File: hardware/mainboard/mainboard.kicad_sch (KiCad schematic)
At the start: 82 parts, among them J1 USB_C_Receptacle_USB2.0_16P, J2 Conn_01x03_Pin, J3 Barrel_Jack_MountingPin, J4 Conn_01x04_Socket, J5 Conn_01x04_Socket, J6 Screw_Terminal_01x02, J7 Conn_01x02_Socket, J8 Conn_01x02_Socket, J9 Conn_01x04_Socket, Q1 BTN8982TA, Q2 AO3400A, Q3 AO3400A, Q6 BTN8982TA, U1 ESP32-S3-WROOM-1, U2 USBLC6-2SC6, U3 AP2112K-3.3, U4 TPS2116DRL, U5 TPS62161DSG

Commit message: finished component placement
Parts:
- J9: footprint Connector_PinHeader_2.54mm:PinHeader_1x04_P2.54mm_Vertical -> Connector_PinSocket_2.54mm:PinSocket_1x04_P2.54mm_Vertical
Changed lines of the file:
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@@
 			)
 		)
-		(property "Footprint" "Connector_PinHeader_2.54mm:PinHeader_1x04_P2.54mm_Vertical"
+		(property "Footprint" "Connector_PinSocket_2.54mm:PinSocket_1x04_P2.54mm_Vertical"
 			(at 184.15 95.25 0)
 			(effects

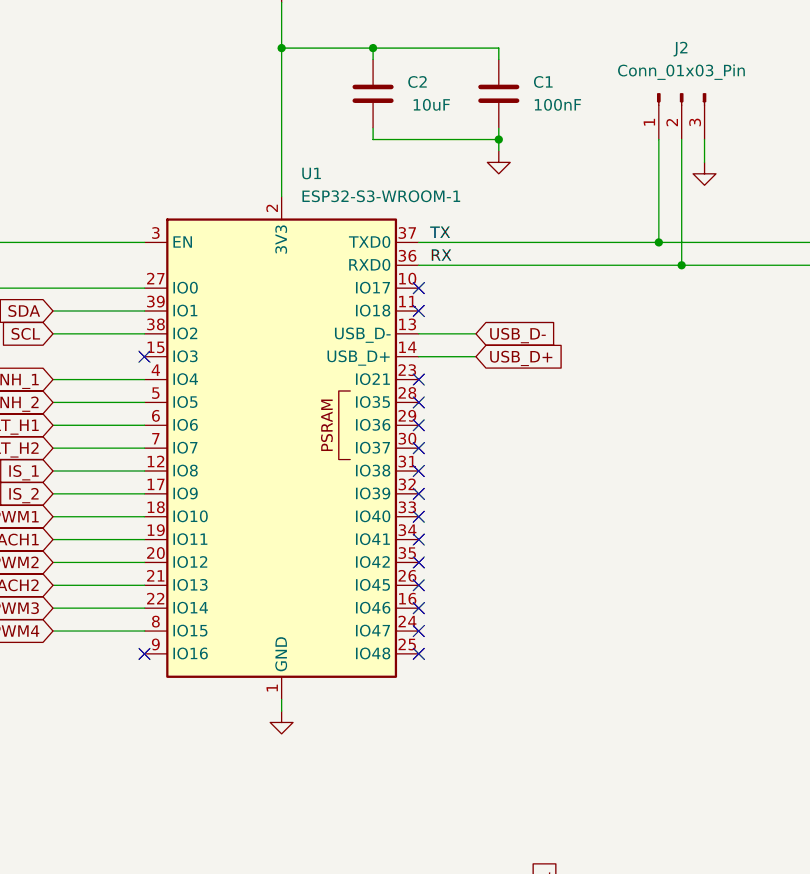
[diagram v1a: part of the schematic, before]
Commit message: signal routing for pwm fans and h-bridge
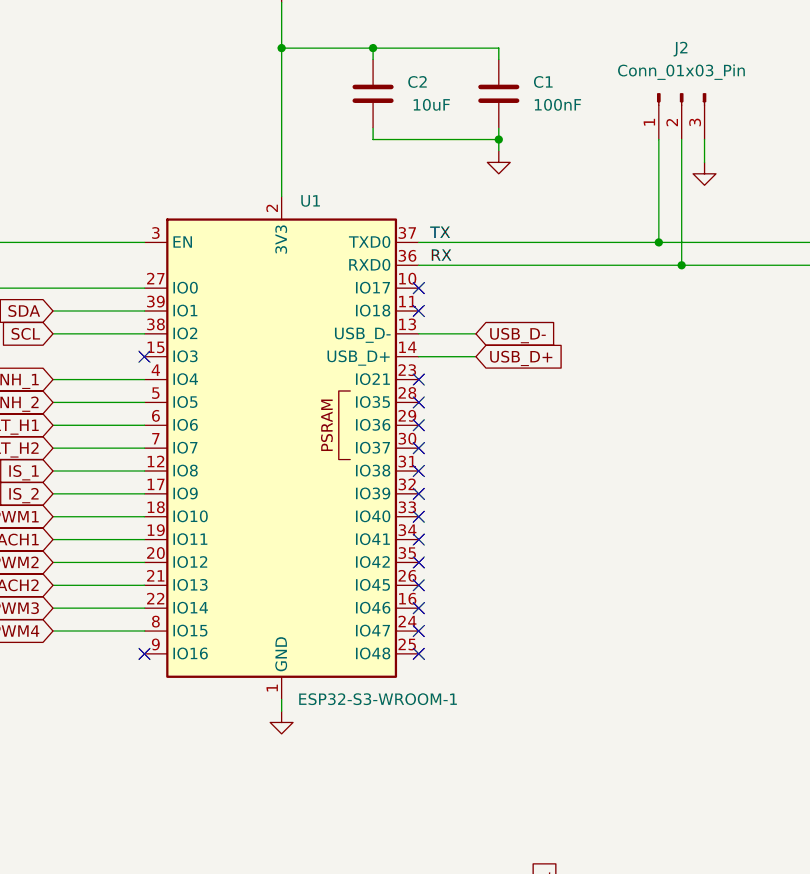
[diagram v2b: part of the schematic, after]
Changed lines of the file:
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@@
 		(on_board yes)
 		(dnp no)
-		(fields_autoplaced yes)
 		(property "Reference" "U1"
-			(at 91.0433 45.72 0)
+			(at 90.932 48.768 0)
 			(effects
 				(font
@@
 		)
 		(property "Value" "ESP32-S3-WROOM-1"
-			(at 91.0433 48.26 0)
+			(at 90.678 104.14 0)
 			(effects
 				(font

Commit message: revised routing and power stage routing
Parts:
- added H1, H2, H3: MountingHole_Pad, MountingHole:MountingHole_2.2mm_M2_Pad_TopBottom, symbol Mechanical:MountingHole_Pad
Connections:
- net GND: now also H1.1, H2.1, H3.1

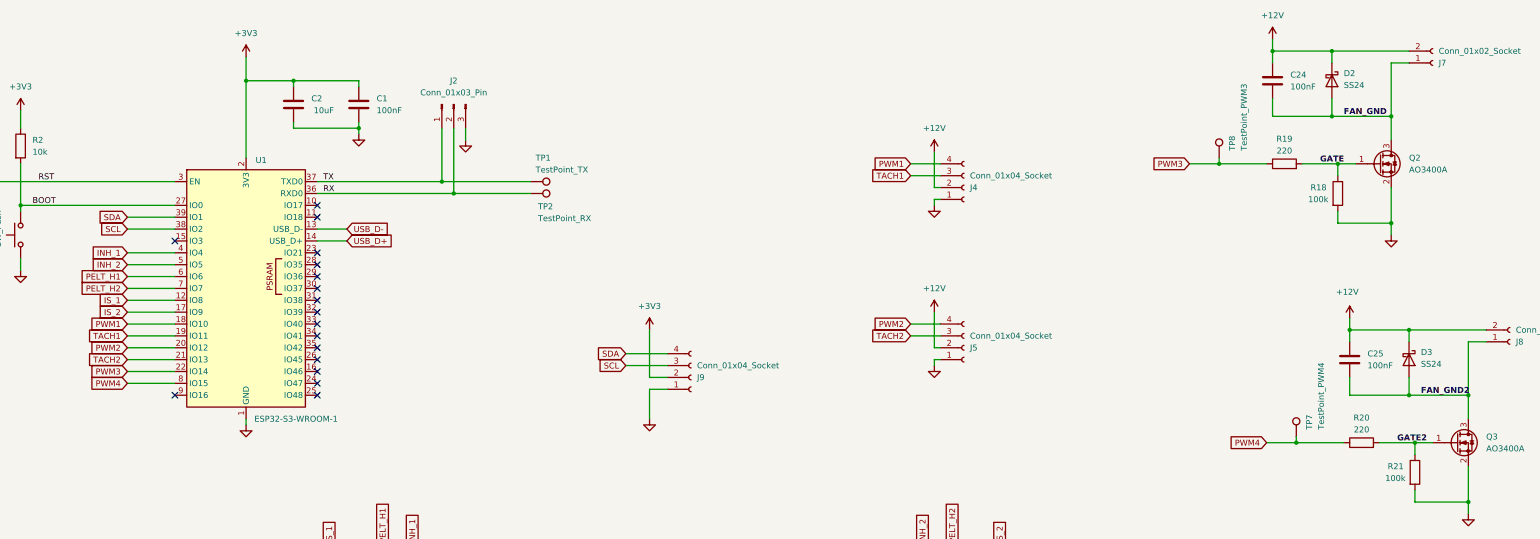
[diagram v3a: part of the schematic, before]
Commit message: routing reworks; adjusted display position, silkscreen adjustments
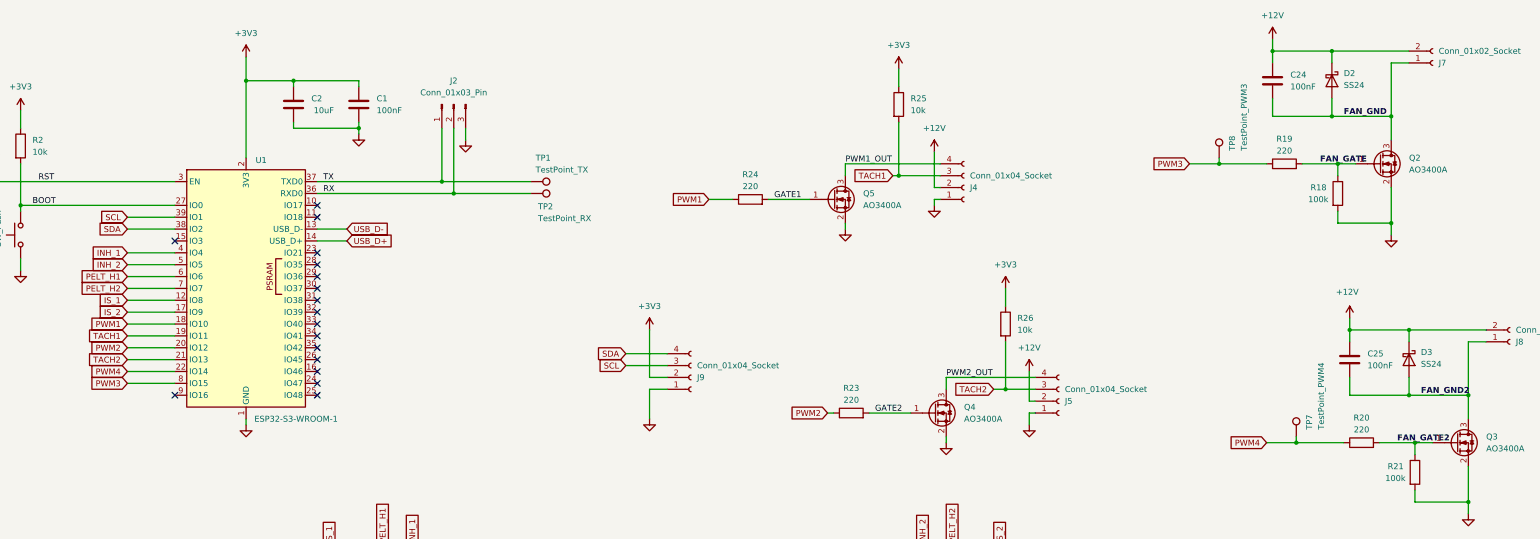
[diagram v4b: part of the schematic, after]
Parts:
- added Q4, Q5: AO3400A, Package_TO_SOT_SMD:SOT-23, symbol Transistor_FET:AO3400A
- added R23, R24: 220, Resistor_SMD:R_0603_1608Metric, symbol Device:R
- added R25, R26: 10k, Resistor_SMD:R_0603_1608Metric, symbol Device:R
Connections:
- net +3V3: now also R25.1, R26.1
- net GATE2: now also Q4.1 (G), R23.2; no longer Q3.1 (G), R20.2, R21.1
- net GND: now also Q4.2 (S), Q5.2 (S)
- net PWM1: now also R24.1; no longer J4.4 (Pin_4)
- net PWM2: now also R23.1; no longer J5.4 (Pin_4)
- net PWM3: now also U1.8 (IO15); no longer U1.22 (IO14)
- net PWM4: now also U1.22 (IO14); no longer U1.8 (IO15)
- net SCL: now also U1.39 (IO1); no longer U1.38 (IO2)
- net SDA: now also U1.38 (IO2); no longer U1.39 (IO1)
- net TACH1: now also R25.2
- net TACH2: now also R26.2
- net GATE renamed FAN_GATE
- new net FAN_GATE2: Q3.1 (G), R20.2, R21.1
- new net GATE1: Q5.1 (G), R24.2
- new net PWM1_OUT: J4.4 (Pin_4), Q5.3 (D)
- new net PWM2_OUT: J5.4 (Pin_4), Q4.3 (D)
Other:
- moved on the sheet: J5
